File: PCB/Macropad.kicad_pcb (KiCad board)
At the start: 2 copper layers, 64 x 73 mm, 31 parts, among them J1 OLED, SW1 SW_Push, SW11 RotaryEncoder_Switch, SW2 SW_Push, SW3 SW_Push, SW4 SW_Push, SW5 SW_Push, SW6 SW_Push, SW7 SW_Push, SW8 SW_Push, SW9 SW_Push, U1 XIAO-RP2040-DIP

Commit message: Update PCB files
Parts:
- removed D1, D13, D14, D15, D16, D17, D2, D6: SK6812MINI, LED_SMD:LED_SK6812MINI_PLCC4_3.5x3.5mm_P1.75mm
- removed J1: OLED, KiCad-SSD1306-0.91-OLED-4pin-128x32.pretty-master:SSD1306-0.91-OLED-4pin-128x32
- removed the REF** at (49.2, 148.1)
- added LED1: MX_SK6812MINI-E, PCM_marbastlib-choc:LED_choc_6028R, B.Cu at (45.9, 139.4)
- added LED2: MX_SK6812MINI-E, PCM_marbastlib-choc:LED_choc_6028R, B.Cu at (46.0, 85.0)
- added LED3: MX_SK6812MINI-E, PCM_marbastlib-choc:LED_choc_6028R, B.Cu at (46.0, 94.5)
- added LED4: MX_SK6812MINI-E, PCM_marbastlib-choc:LED_choc_6028R, B.Cu at (45.9, 103.4)
- added LED5: MX_SK6812MINI-E, PCM_marbastlib-choc:LED_choc_6028R, B.Cu at (45.9, 112.4)
- added LED6: MX_SK6812MINI-E, PCM_marbastlib-choc:LED_choc_6028R, B.Cu at (45.9, 121.4)
- added LED7: MX_SK6812MINI-E, PCM_marbastlib-choc:LED_choc_6028R, B.Cu at (45.9, 130.4)
- added LED8: MX_SK6812MINI-E, PCM_marbastlib-choc:LED_choc_6028R, B.Cu at (45.9, 148.4)
- added REF**: OSHW-Logo_5.7x6mm_SilkScreen, Symbol:OSHW-Logo_5.7x6mm_SilkScreen, B.Cu at (99.3, 149.0)
- moved G*** 0.13 mm to (84.5, 125.1)
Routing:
- net GND: track 118.5 -> 132.4 mm, vias 1 -> 0
- net Net-(D1-DOUT): track 6.76 -> 0.00 mm
- net Net-(D14-DOUT): track 6.71 -> 0.00 mm
- net Net-(D2-DOUT): track 6.65 -> 0.00 mm
- net Net-(D15-DOUT): track 6.65 -> 0.00 mm
- net Net-(D13-DOUT): track 6.65 -> 0.00 mm
- net Net-(D13-DIN): track 6.65 -> 0.00 mm
- net Net-(D16-DOUT): track 6.65 -> 0.00 mm
- net +5V: track 85.2 -> 79.8 mm, vias 1 -> 0
- net Net-(LED2-DOUT): track 0.00 -> 4.63 mm
- net Net-(LED3-DOUT): track 0.00 -> 4.18 mm
- net Net-(LED1-DIN): track 0.00 -> 4.16 mm
- net Net-(LED6-DOUT): track 0.00 -> 4.16 mm
- net Net-(LED5-DOUT): track 0.00 -> 4.16 mm
- net Net-(LED1-DOUT): track 0.00 -> 4.16 mm
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
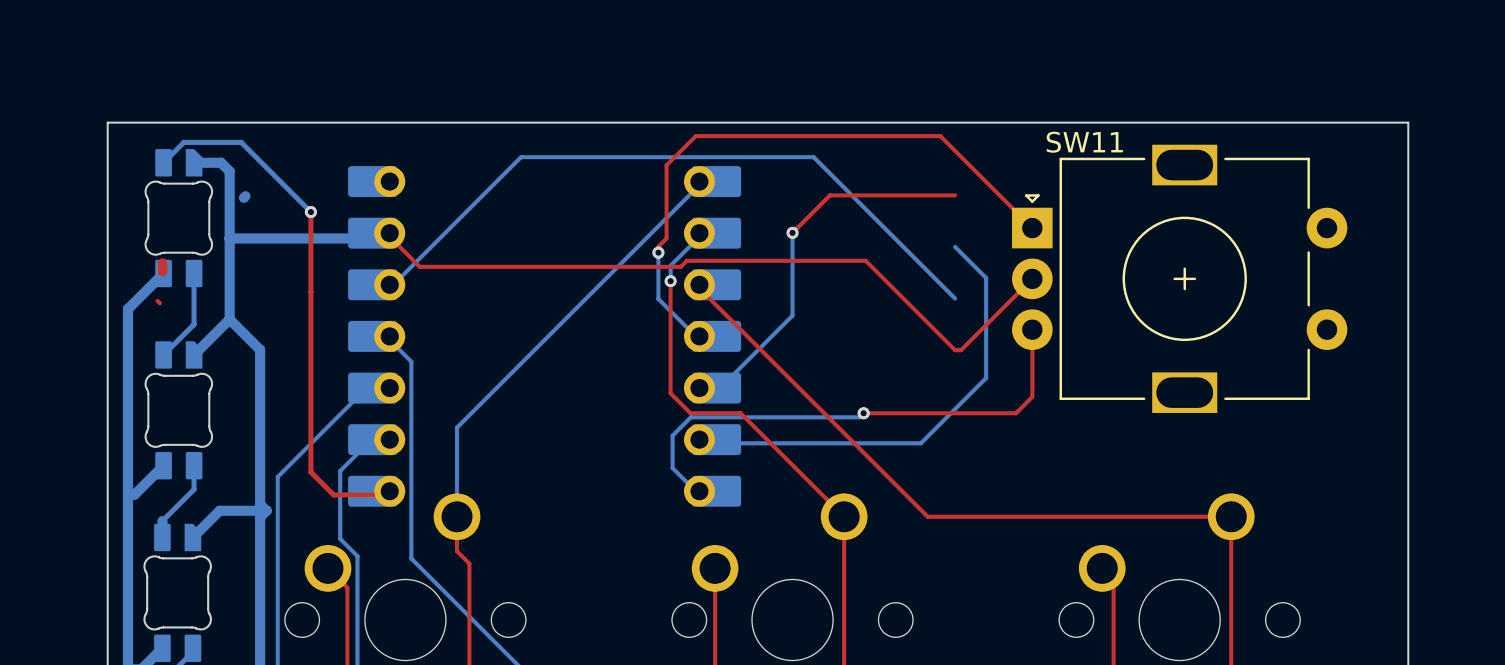
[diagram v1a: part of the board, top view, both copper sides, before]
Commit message: Fixed some bugs in the PCB and exported Gerber files.
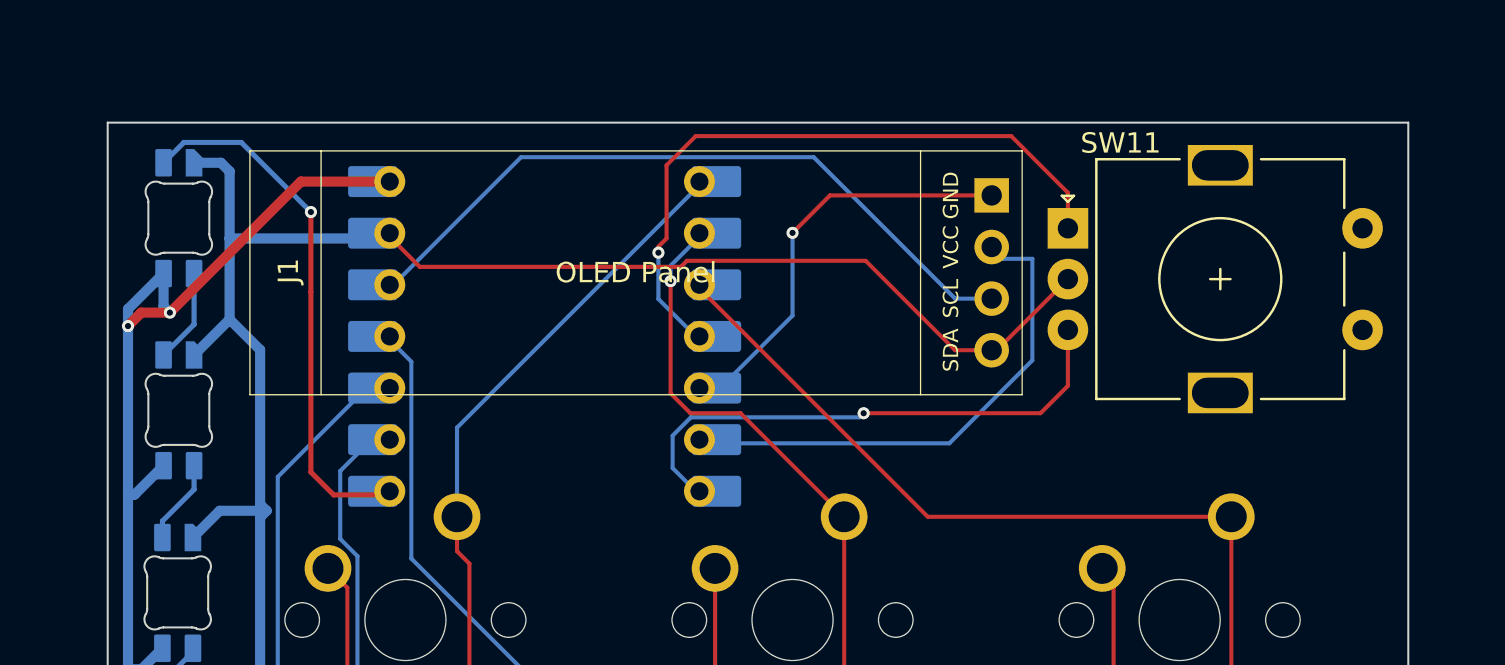
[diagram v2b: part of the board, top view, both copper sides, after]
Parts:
- added J1: OLED, KiCad-SSD1306-0.91-OLED-4pin-128x32.pretty-master:SSD1306-0.91-OLED-4pin-128x32, F.Cu at (49.5, 81.7)
- moved SW11 1.75 mm to (89.8, 85.5)
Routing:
- net +5V: track 79.8 -> 97.1 mm, vias 0 -> 2
- net /SCL: track 21.7 -> 24.5 mm
- net EN1: track 30.1 -> 32.9 mm
- net /SDA: track 18.1 -> 19.9 mm
- net +3V3: track 33.4 -> 35.2 mm
- net GND: track 132.4 -> 134.0 mm
- net EN2: track 25.5 -> 26.9 mm

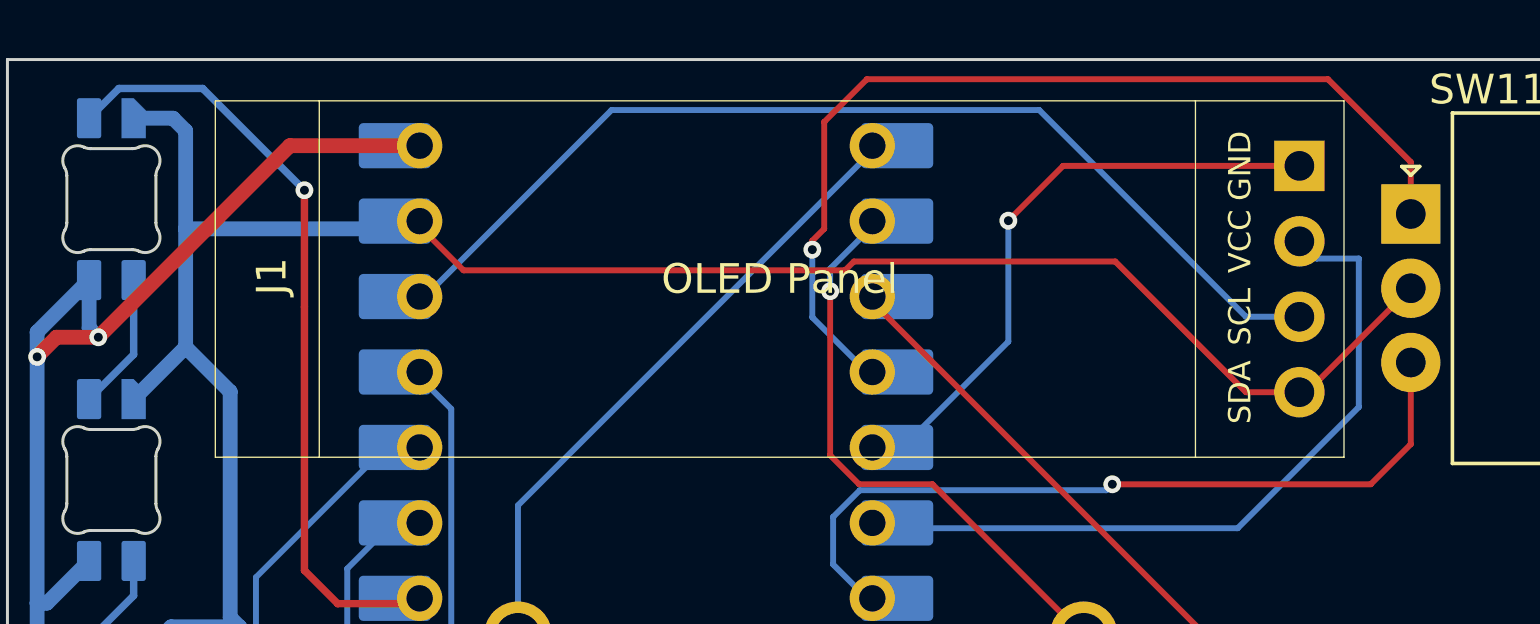
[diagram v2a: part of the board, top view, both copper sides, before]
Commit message: Fixed some bugs in the PCB and exported Gerber files again.
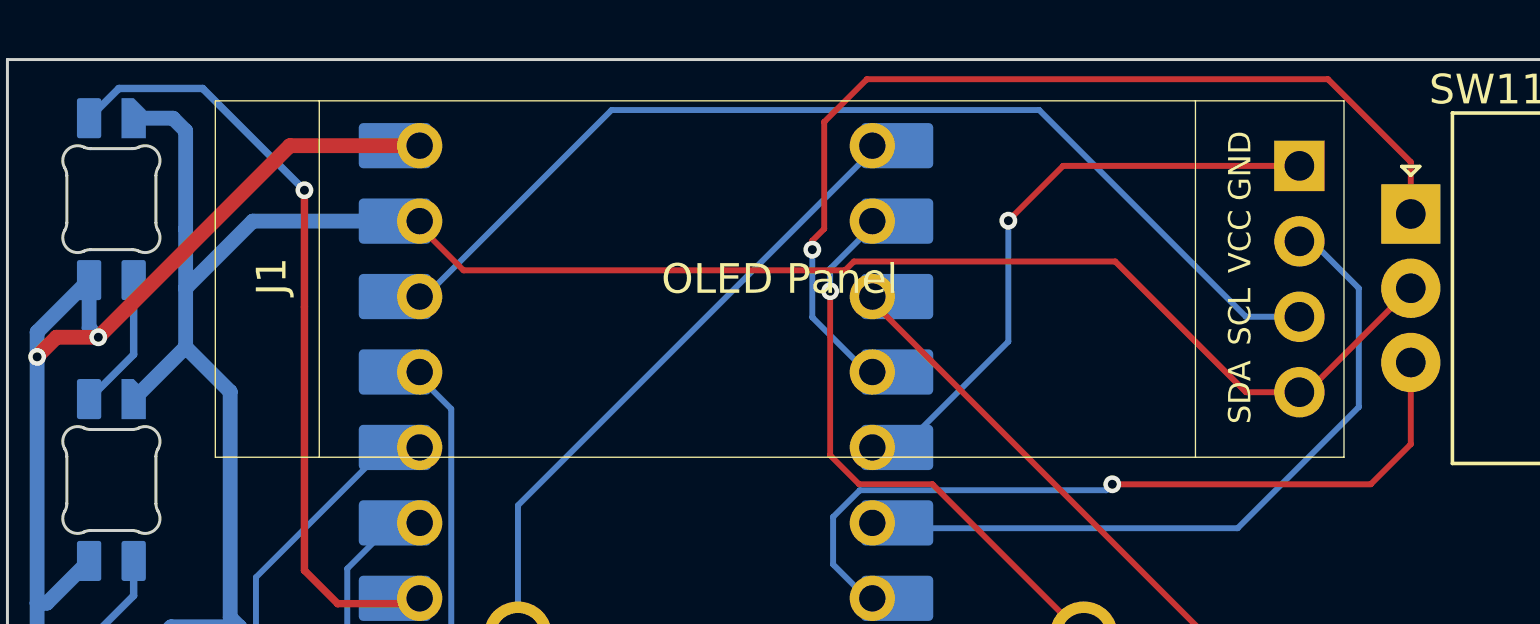
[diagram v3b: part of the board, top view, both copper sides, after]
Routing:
- net GND: track 134.0 -> 135.3 mm
- net /SCL: track 24.5 -> 23.9 mm
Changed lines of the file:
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@@
 			(drillshape 0)
 			(scaleselection 1)
-			(outputdirectory "")
+			(outputdirectory "./")
 		)
 	)
@@
 	)
 	(segment
+		(start 55.545 85.74)
+		(end 50.76 85.74)
+		(width 0.5)
+		(layer "B.Cu")
+		(net 1)
+	)
+	(segment
 		(start 48.5 89.981335)
 		(end 46.75 91.731335)
@@
 	)
 	(segment
+		(start 55.545 85.92)
+		(end 55.28 85.92)
+		(width 0.5)
+		(layer "B.Cu")
+		(net 1)
+	)
+	(segment
 		(start 46.847669 118.838336)
 		(end 47.878764 118.838336)
@@
 	)
 	(segment
-		(start 55.2 86)
-		(end 48.5 86)
-		(width 0.5)
-		(layer "B.Cu")
-		(net 1)
-	)
-	(segment
 		(start 46.69375 145.6375)
 		(end 46.69375 145.40625)
@@
 	(segment
 		(start 48.5 86)
-		(end 48.5 89.981335)
+		(end 48.5 88)
 		(width 0.5)
 		(layer "B.Cu")
@@
 	)
 	(segment
-		(start 55.545 85.92)
-		(end 55.28 85.92)
-		(width 0.5)
-		(layer "B.Cu")
-		(net 1)
-	)
-	(segment
 		(start 49.291804 127.808196)
 		(end 50.1 127)
@@
 	)
 	(segment
+		(start 50.76 85.74)
+		(end 48.5 88)
+		(width 0.5)
+		(layer "B.Cu")
+		(net 1)
+	)
+	(segment
 		(start 48.009446 99.4)
 		(end 50.3171 99.4)
@@
 	)
 	(segment
+		(start 48.5 88)
+		(end 48.5 89.981335)
+		(width 0.5)
+		(layer "B.Cu")
+		(net 1)
+	)
+	(segment
 		(start 49.291804 127.825296)
 		(end 49.291804 127.808196)
@@
 	)
 	(segment
-		(start 72.455 96.08)
-		(end 83.92 96.08)
+		(start 83.92 96.08)
+		(end 88 92)
 		(width 0.2)
 		(layer "B.Cu")
@@
 	)
 	(segment
-		(start 83.92 96.08)
-		(end 88 92)
+		(start 88 92)
+		(end 88 88)
 		(width 0.2)
 		(layer "B.Cu")
@@
 	)
 	(segment
-		(start 86.58 87)
-		(end 86 86.42)
+		(start 72.455 96.08)
+		(end 83.92 96.08)
 		(width 0.2)
 		(layer "B.Cu")
@@
 	)
 	(segment
-		(start 88 87)
-		(end 86.58 87)
+		(start 86.42 86.42)
+		(end 86 86.42)
 		(width 0.2)
 		(layer "B.Cu")
@@
 	)
 	(segment
-		(start 88 92)
-		(end 88 87)
+		(start 88 88)
+		(end 86.42 86.42)
 		(width 0.2)
 		(layer "B.Cu")

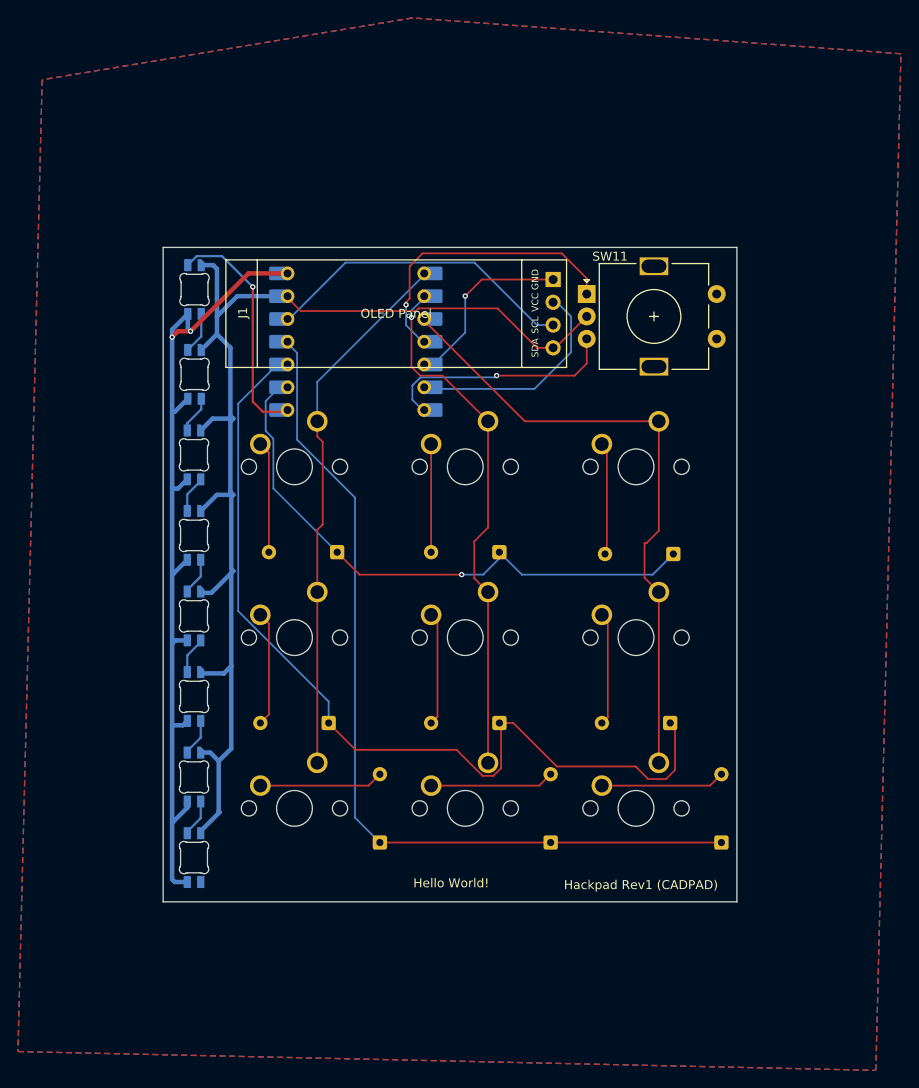
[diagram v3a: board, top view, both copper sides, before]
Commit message: Fixed some bugs in the PCB and exported Gerber files again. CAD files have been updated with the latest modifications.
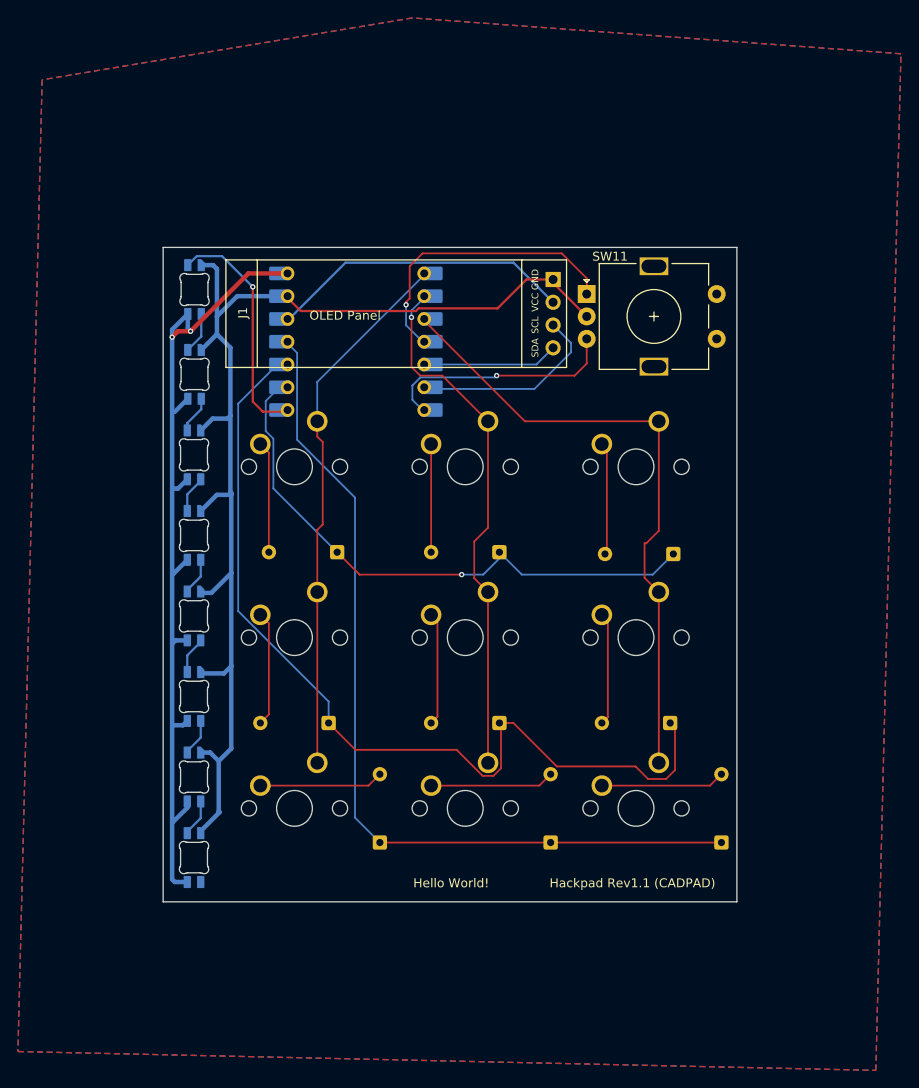
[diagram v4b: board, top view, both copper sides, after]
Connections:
- J1 pad 1: /SDA -> GND
- J1 pad 2: /SCL -> +3V3
- J1 pad 3: +3V3 -> /SCL
- J1 pad 4: GND -> /SDA
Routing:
- net /SDA: track 19.9 -> 15.2 mm, vias 1 -> 0
- net /SCL: track 23.9 -> 21.1 mm
- net Column 1: track 60.5 -> 58.7 mm
- net GND: track 135.3 -> 133.6 mm
- net +3V3: track 35.2 -> 34.5 mm
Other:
- board text added: "Hackpad Rev1.1 (CADPAD)"
- board text removed: "Hackpad Rev1 (CADPAD)"
